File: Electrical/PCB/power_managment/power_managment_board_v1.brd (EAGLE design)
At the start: 160 x 100 mm, 1 part

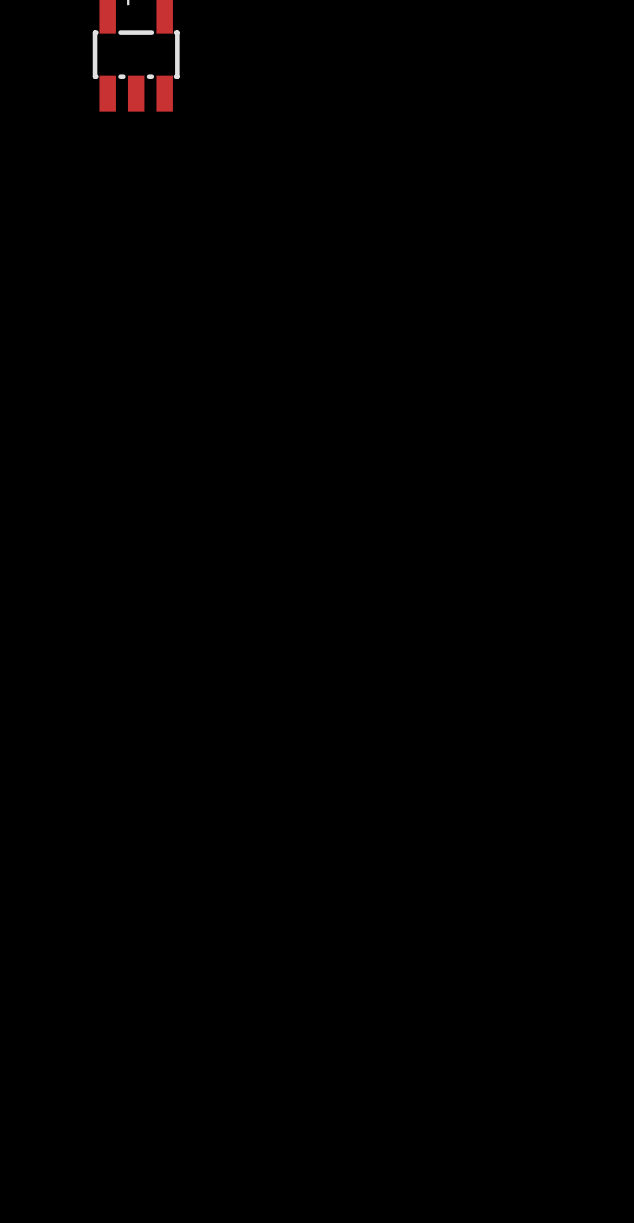
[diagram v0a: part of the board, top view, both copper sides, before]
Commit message: Imported a diode library
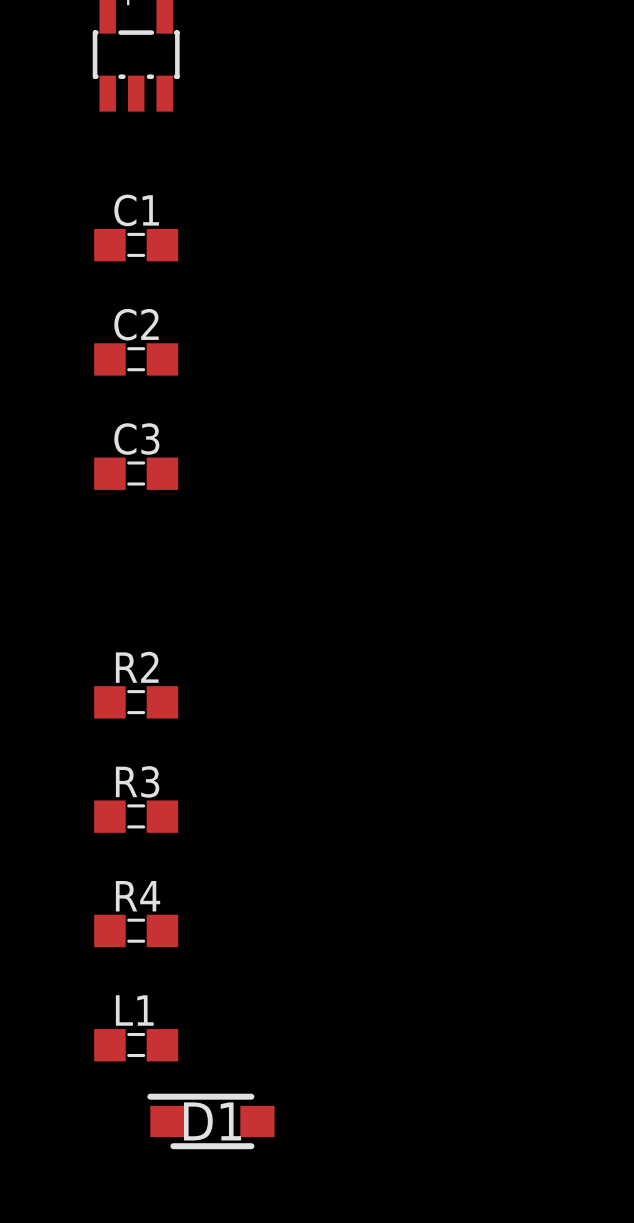
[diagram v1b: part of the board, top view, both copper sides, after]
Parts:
- added C1, C2, C3, L1, R2, R3, R4: (no value), RobotRacing2019_Master:0603SMT
- added D1: CRS08(TE85L,Q,M), SamacSys_Parts:SODFL3516X108N
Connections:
- new net GND: C1.2, C2.2, R3.2, R4.2, U$1.2, U$1.4
- new net N$1: C1.1, L1.1, R4.1, U$1.5
- new net N$2: C2.1, C3.2, D1.1, R2.1
- new net N$3: C3.1, R2.2, R3.1, U$1.3
- new net N$4: D1.2, L1.2, U$1.1
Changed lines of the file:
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@@
 <attribute name="VALUE" x="0.635" y="-7.239" size="1.27" layer="27"/>
+</element>
+<element name="C1" library="RobotRacing2019_Master" package="0603SMT" value="" x="2.54" y="-10.16" smashed="yes">
+<attribute name="NAME" x="1.74" y="-9.51" size="1.016" layer="25"/>
+<attribute name="VALUE" x="1.74" y="-11.81" size="1.016" layer="27"/>
+</element>
+<element name="C2" library="RobotRacing2019_Master" package="0603SMT" value="" x="2.54" y="-13.97" smashed="yes">
+<attribute name="NAME" x="1.74" y="-13.32" size="1.016" layer="25"/>
+<attribute name="VALUE" x="1.74" y="-15.62" size="1.016" layer="27"/>
+</element>
+<element name="C3" library="RobotRacing2019_Master" package="0603SMT" value="" x="2.54" y="-17.78" smashed="yes">
+<attribute name="NAME" x="1.74" y="-17.13" size="1.016" layer="25"/>
+<attribute name="VALUE" x="1.74" y="-19.43" size="1.016" layer="27"/>
+</element>
+<element name="R2" library="RobotRacing2019_Master" package="0603SMT" value="" x="2.54" y="-25.4" smashed="yes">
+<attribute name="NAME" x="1.74" y="-24.75" size="1.016" layer="25"/>
+<attribute name="VALUE" x="1.74" y="-27.05" size="1.016" layer="27"/>
+</element>
+<element name="R3" library="RobotRacing2019_Master" package="0603SMT" value="" x="2.54" y="-29.21" smashed="yes">
+<attribute name="NAME" x="1.74" y="-28.56" size="1.016" layer="25"/>
+<attribute name="VALUE" x="1.74" y="-30.86" size="1.016" layer="27"/>
+</element>
+<element name="R4" library="RobotRacing2019_Master" package="0603SMT" value="" x="2.54" y="-33.02" smashed="yes">
+<attribute name="NAME" x="1.74" y="-32.37" size="1.016" layer="25"/>
+<attribute name="VALUE" x="1.74" y="-34.67" size="1.016" layer="27"/>
+</element>
+<element name="L1" library="RobotRacing2019_Master" package="0603SMT" value="" x="2.54" y="-36.83" smashed="yes">
+<attribute name="NAME" x="1.74" y="-36.18" size="1.016" layer="25"/>
+<attribute name="VALUE" x="1.74" y="-38.48" size="1.016" layer="27"/>
+</element>
+<element name="D1" library="SamacSys_Parts" package="SODFL3516X108N" value="CRS08(TE85L,Q,M)" x="5.08" y="-39.37" smashed="yes">
+<attribute name="DESCRIPTION" value="Schottky Rectifier 30V 1.5A 0.36V S-FLAT" x="5.08" y="-39.37" size="1.778" layer="27" display="off"/>
+<attribute name="HEIGHT" value="1.08mm" x="5.08" y="-39.37" size="1.778" layer="27" display="off"/>
+<attribute name="MANUFACTURER_NAME" value="Toshiba" x="5.08" y="-39.37" size="1.778" layer="27" display="off"/>
+<attribute name="MANUFACTURER_PART_NUMBER" value="CRS08(TE85L,Q,M)" x="5.08" y="-39.37" size="1.778" layer="27" display="off"/>
+<attribute name="MOUSER_PART_NUMBER" value="757-CRS08TE85LQM" x="5.08" y="-39.37" size="1.778" layer="27" display="off"/>
+<attribute name="NAME" x="5.08" y="-39.37" size="1.27" layer="25" align="center"/>
+<attribute name="VALUE" x="5.08" y="-39.37" size="1.27" layer="27" align="center"/>
 </element>
 </elements>
 <signals>
+<signal name="N$1">
+<contactref element="U$1" pad="5"/>
+<contactref element="R4" pad="1"/>
+<contactref element="C1" pad="1"/>
+<contactref element="L1" pad="1"/>
+<wire x1="1.665" y1="-33.02" x2="1.665" y2="-36.83" width="0" layer="19" extent="1-1"/>
+<wire x1="1.665" y1="-10.16" x2="1.665" y2="-33.02" width="0" layer="19" extent="1-1"/>
+<wire x1="1.59" y1="-2.51" x2="1.665" y2="-10.16" width="0" layer="19" extent="1-1"/>
+</signal>
+<signal name="GND">
+<contactref element="U$1" pad="2"/>
+<contactref element="R3" pad="2"/>
+<contactref element="R4" pad="2"/>
+<contactref element="U$1" pad="4"/>
+<contactref element="C1" pad="2"/>
+<contactref element="C2" pad="2"/>
+<wire x1="3.415" y1="-29.21" x2="3.415" y2="-33.02" width="0" layer="19" extent="1-1"/>
+<wire x1="3.415" y1="-13.97" x2="3.415" y2="-29.21" width="0" layer="19" extent="1-1"/>
+<wire x1="3.415" y1="-10.16" x2="3.415" y2="-13.97" width="0" layer="19" extent="1-1"/>
+<wire x1="2.54" y1="-5.11" x2="3.415" y2="-10.16" width="0" layer="19" extent="1-1"/>
+<wire x1="3.49" y1="-2.51" x2="2.54" y2="-5.11" width="0" layer="19" extent="1-1"/>
+</signal>
+<signal name="N$2">
+<contactref element="C3" pad="2"/>
+<contactref element="C2" pad="1"/>
+<contactref element="R2" pad="1"/>
+<contactref element="D1" pad="1"/>
+<wire x1="1.665" y1="-25.4" x2="3.58" y2="-39.37" width="0" layer="19" extent="1-1"/>
+<wire x1="3.415" y1="-17.78" x2="1.665" y2="-25.4" width="0" layer="19" extent="1-1"/>
+<wire x1="1.665" y1="-13.97" x2="3.415" y2="-17.78" width="0" layer="19" extent="1-1"/>
+</signal>
+<signal name="N$3">
+<contactref element="R3" pad="1"/>
+<contactref element="U$1" pad="3"/>
+<contactref element="C3" pad="1"/>
+<contactref element="R2" pad="2"/>
+<wire x1="3.415" y1="-25.4" x2="1.665" y2="-29.21" width="0" layer="19" extent="1-1"/>
+<wire x1="1.665" y1="-17.78" x2="3.415" y2="-25.4" width="0" layer="19" extent="1-1"/>
+<wire x1="3.49" y1="-5.11" x2="1.665" y2="-17.78" width="0" layer="19" extent="1-1"/>
+</signal>
+<signal name="N$4">
+<contactref element="L1" pad="2"/>
+<contactref element="U$1" pad="1"/>
+<contactref element="D1" pad="2"/>
+<wire x1="6.58" y1="-39.37" x2="3.415" y2="-36.83" width="0" layer="19" extent="1-1"/>
+<wire x1="1.59" y1="-5.11" x2="3.415" y2="-36.83" width="0" layer="19" extent="1-1"/>
+</signal>
 </signals>
 <mfgpreviewcolors>

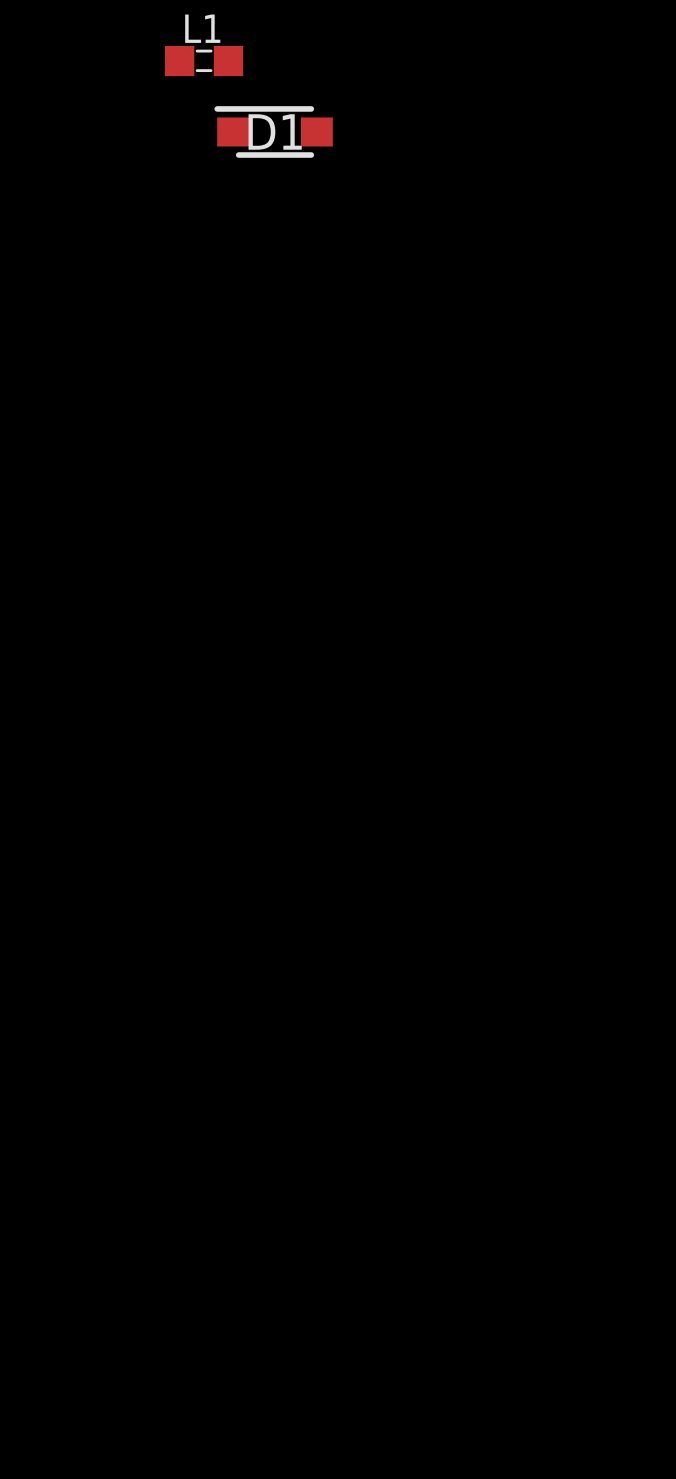
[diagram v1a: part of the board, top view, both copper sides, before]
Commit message: Updated the SVS for 11.1V
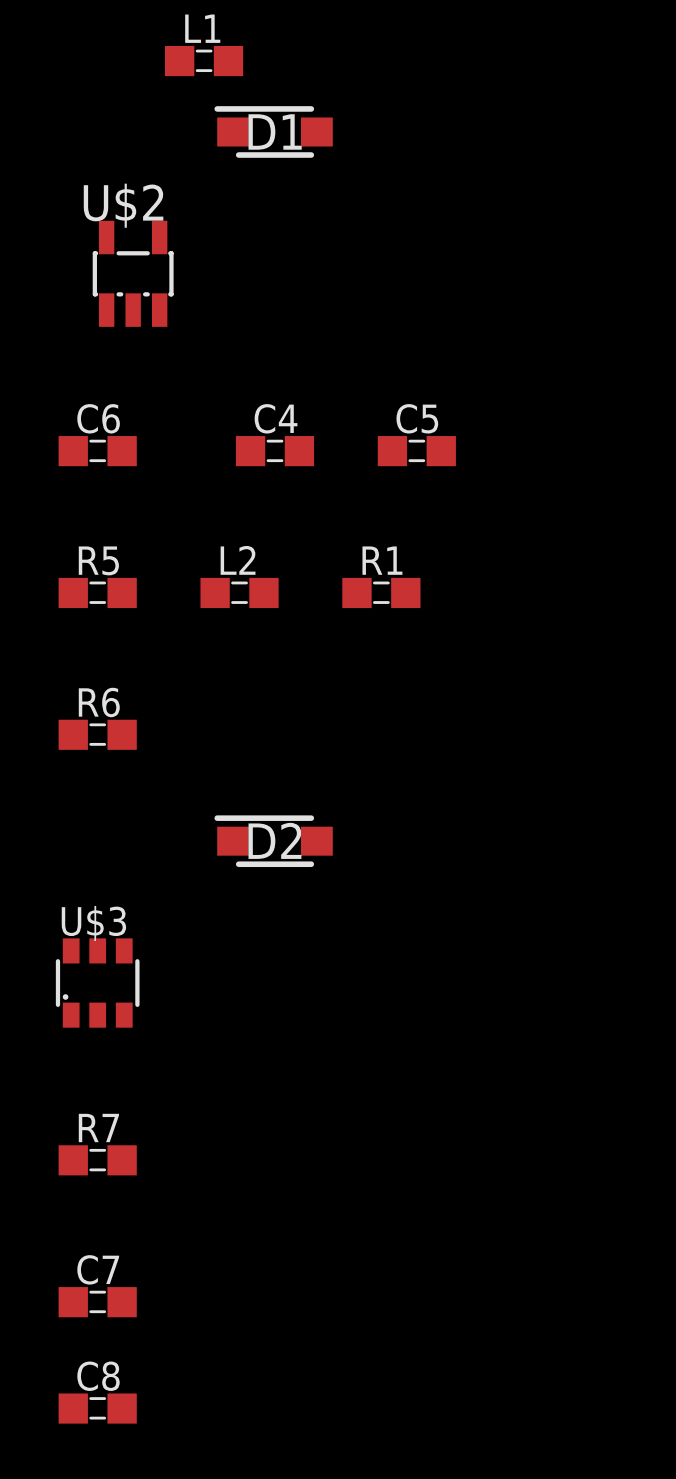
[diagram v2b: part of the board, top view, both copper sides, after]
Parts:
- added C4: 2.2uF, RobotRacing2019_Master:0603SMT
- added C5: 4.7uF, RobotRacing2019_Master:0603SMT
- added C6: 160pF, RobotRacing2019_Master:0603SMT
- added C7: TBA (Probably OPEN), RobotRacing2019_Master:0603SMT
- added C8: TBA, RobotRacing2019_Master:0603SMT
- added D2: CRS08(TE85L,Q,M), SamacSys_Parts:SODFL3516X108N
- added L2: 10uH, RobotRacing2019_Master:0603SMT
- added R1: 124k, RobotRacing2019_Master:0603SMT
- added R5: 13.3k, RobotRacing2019_Master:0603SMT
- added R6: 51k, RobotRacing2019_Master:0603SMT
- added R7: 100k, RobotRacing2019_Master:0603SMT
- added U$2: LMR64010SOT, RobotRacing2019_Master:SOT23-5
- added U$3: S-1011AA0SOT, RobotRacing2019_Master:SOT23-6
- C1: value (none) -> 2.2uF
- C2: value (none) -> 4.7uF
- C3: value (none) -> 160pF
- L1: value (none) -> 10uH
- R2: value (none) -> 124k
- R3: value (none) -> 13.3k
- R4: value (none) -> 51k
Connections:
- removed net N$1: C1.1, L1.1, R4.1, U$1.5
- new net N$10: R7.1, U$3.3
- new net N$12: C8.1, U$3.6
- new net N$13: C7.1, U$3.4
- new net N$6: C5.1, C6.2, D2.1, R1.1
- new net N$7: C6.1, R1.2, R5.1, U$2.3
- new net N$8: D2.2, L2.2, U$2.1
- new net VDD: C1.1, C4.1, L1.1, L2.1, R4.1, R6.1, R7.2, U$1.5, U$2.5, U$3.1
- net GND: now also C4.2, C5.2, C7.2, C8.2, R5.2, R6.2, U$2.2, U$2.4, U$3.5
